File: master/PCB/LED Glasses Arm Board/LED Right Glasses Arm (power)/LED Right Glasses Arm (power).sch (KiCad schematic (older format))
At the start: 24 parts, among them J1 Conn_01x02_Male, J2 Conn_01x01_Male, J3 Conn_01x01_Male, Q1 TP0610T, SW1 SW_SPST, U1 TPS63060

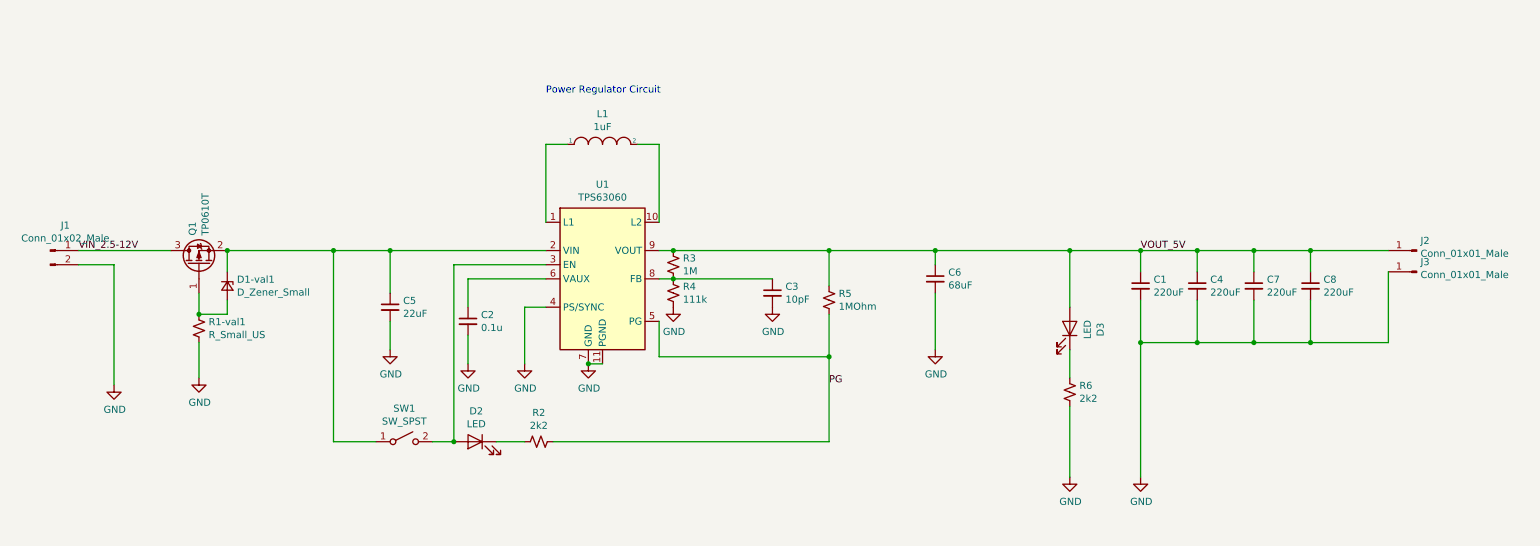
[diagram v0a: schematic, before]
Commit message: Updated with all components with links
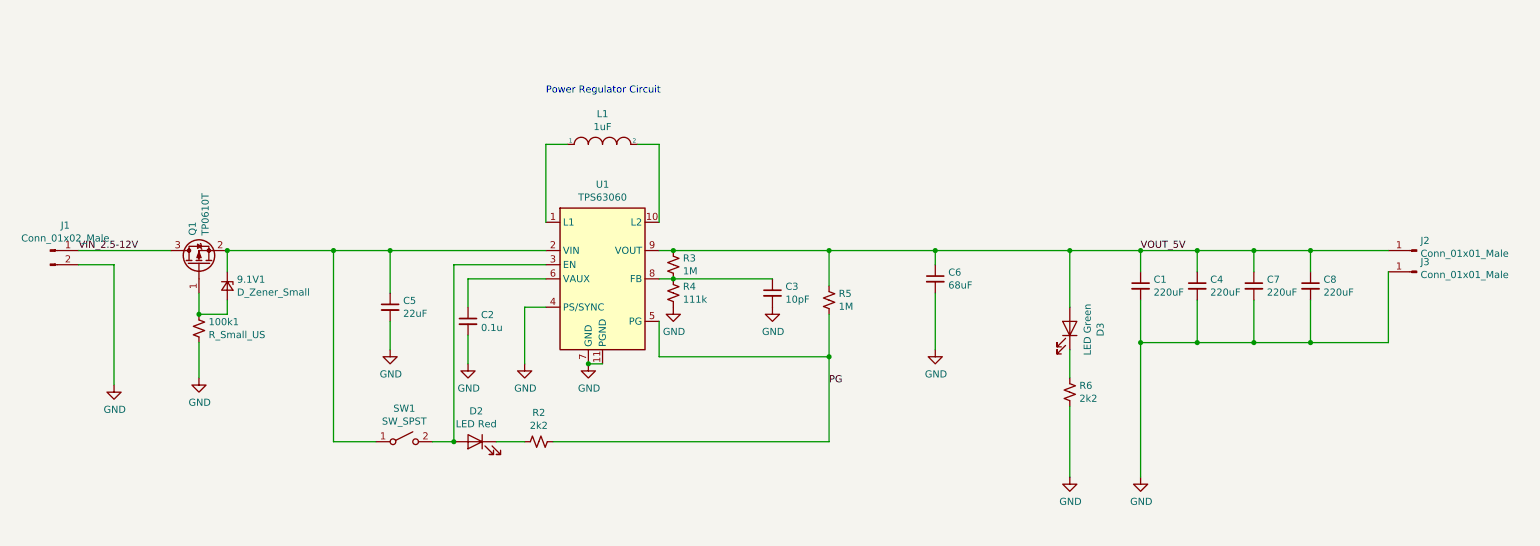
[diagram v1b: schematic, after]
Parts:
- 100k1: renamed from R1-val1; Digikey Link (none) -> https://www.digikey.com.au/product-detail/en/susumu/RR0816P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
- 9.1V1: renamed from D1-val1; Digikey link (none) -> https://www.digikey.com.au/product-detail/en/comchip-techno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
- D2: value LED -> LED Red; Digikey Link (none) -> https://www.digikey.com.au/product-detail/en/lite-on-inc/LT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
- D3: value LED -> LED Green; Digikey Link (none) -> https://www.digikey.com.au/product-detail/en/lite-on-inc/LT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
- L1: footprint Inductor_SMD:L_Coilcraft_XxL4020 -> sft:SRN4018TA; Digikey (none) -> https://www.digikey.com/en/products/detail/bourns-inc/SRN40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; Link XFL4020-102MEC -> (none); Old product (none) -> XFL4020-102MEC; element14 https://au.element14.com/coilcraft/xfl4020-102mec/inductor-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 -> (none)
- Q1: Link https://au.element14.com/vishay/si2315bds-t1-ge3/p-channel-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 -> (none)
- R2, R6: Digikey Link (none) -> https://www.digikey.com.au/product-detail/en/te-connectivit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
- R4: footprint Resistor_SMD:R_0603_1608Metric -> Resistor_SMD:R_0805_2012Metric; Digikey Link (none) -> https://www.digikey.com.au/product-detail/en/vishay-thin-fi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
- R5: value 1MOhm -> 1M
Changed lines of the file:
@@
 F 0 "L1" H 4750 3515 50  0000 C CNN
 F 1 "1uF" H 4750 3424 50  0000 C CNN
-F 2 "Inductor_SMD:L_Coilcraft_XxL4020" H 4750 3300 50  0001 C CNN
-F 3 "http://www.farnell.com/datasheets/1682010.pdf" H 4750 3300 50  0001 C CNN
-F 4 "XFL4020-102MEC" H 4750 3300 50  0001 C CNN "Link"
-F 5 "https://au.element14.com/coilcraft/xfl4020-102mec/inductor-1uh-11a-20-pwr-64mhz/dp/2289214?st=xfl4020-102mec" H 4750 3300 50  0001 C CNN "element14"
+F 2 "sft:SRN4018TA" H 4750 3300 50  0001 C CNN
+F 3 "https://www.bourns.com/docs/Product-Datasheets/SRN4018TA.pdf" H 4750 3300 50  0001 C CNN
+F 4 "XFL4020-102MEC" H 4750 3300 50  0001 C CNN "Old product"
+F 5 "https://www.digikey.com/en/products/detail/bourns-inc/SRN4018TA-1R0M/6565079" H 4750 3300 50  0001 C CNN "Digikey"
 	1    4750 3300
 	1    0    0    -1
@@
 F 1 "1M" H 5318 4105 50  0000 L CNN
 F 2 "Resistor_SMD:R_0603_1608Metric" H 5250 4150 50  0001 C CNN
-F 3 "~" H 5250 4150 50  0001 C CNN
+F 3 "https://www.yageo.com/upload/media/product/productsearch/datasheet/rchip/PYu-RT_1-to-0.01_RoHS_L_12.pdf" H 5250 4150 50  0001 C CNN
 F 4 "https://www.digikey.com.au/product-detail/en/yageo/RT0603BRD071ML/YAG4498CT-ND/6616654" H 5250 4150 50  0001 C CNN "Digikey Link"
 	1    5250 4150
@@
 F 0 "R4" H 5318 4396 50  0000 L CNN
 F 1 "111k" H 5318 4305 50  0000 L CNN
-F 2 "Resistor_SMD:R_0603_1608Metric" H 5250 4350 50  0001 C CNN
-F 3 "~" H 5250 4350 50  0001 C CNN
+F 2 "Resistor_SMD:R_0805_2012Metric" H 5250 4350 50  0001 C CNN
+F 3 "https://www.vishay.com/docs/60026/ptn.pdf" H 5250 4350 50  0001 C CNN
+F 4 "https://www.digikey.com.au/product-detail/en/vishay-thin-film/PTN0805E1113BST1/764-1475-6-ND/7103531" H 5250 4350 50  0001 C CNN "Digikey Link"
 	1    5250 4350
 	1    0    0    -1
@@
 P 6350 4400
 F 0 "R5" H 6418 4446 50  0000 L CNN
-F 1 "1MOhm" H 6418 4355 50  0000 L CNN
+F 1 "1M" H 6418 4355 50  0000 L CNN
 F 2 "Resistor_SMD:R_0603_1608Metric" H 6350 4400 50  0001 C CNN
-F 3 "~" H 6350 4400 50  0001 C CNN
+F 3 "https://www.yageo.com/upload/media/product/productsearch/datasheet/rchip/PYu-RT_1-to-0.01_RoHS_L_12.pdf" H 6350 4400 50  0001 C CNN
 F 4 "https://www.digikey.com.au/product-detail/en/yageo/RT0603BRD071ML/YAG4498CT-ND/6616654" H 6350 4400 50  0001 C CNN "Digikey Link"
 	1    6350 4400
@@
 P 8050 4600
 F 0 "D3" H 8042 4816 50  0000 C CNN
-F 1 "LED" H 8042 4725 50  0000 C CNN
+F 1 "LED Green" H 8042 4725 50  0000 C CNN
 F 2 "LED_SMD:LED_0603_1608Metric" H 8050 4600 50  0001 C CNN
-F 3 "~" H 8050 4600 50  0001 C CNN
+F 3 "https://optoelectronics.liteon.com/upload/download/DS22-2000-226/LTST-S270KGKT.pdf" H 8050 4600 50  0001 C CNN
+F 4 "https://www.digikey.com.au/product-detail/en/lite-on-inc/LTST-S270KGKT/160-1478-1-ND/386892" H 8050 4600 50  0001 C CNN "Digikey Link"
 	1    8050 4600
 	0    1    -1   0
@@
 F 1 "2k2" H 8118 5005 50  0000 L CNN
 F 2 "Resistor_SMD:R_0603_1608Metric" H 8050 5050 50  0001 C CNN
-F 3 "~" H 8050 5050 50  0001 C CNN
+F 3 "https://www.te.com/commerce/DocumentDelivery/DDEController?Action=srchrtrv&DocNm=1773204-3&DocType=DS&DocLang=English" H 8050 5050 50  0001 C CNN
+F 4 "https://www.digikey.com.au/product-detail/en/te-connectivity-passive-product/CRGCQ0603J2K2/A130093CT-ND/8577925" H 8050 5050 50  0001 C CNN "Digikey Link"
 	1    8050 5050
 	1    0    0    -1
@@
 P 3850 5400
 F 0 "D2" H 3842 5616 50  0000 C CNN
-F 1 "LED" H 3842 5525 50  0000 C CNN
+F 1 "LED Red" H 3842 5525 50  0000 C CNN
 F 2 "LED_SMD:LED_0603_1608Metric" H 3850 5400 50  0001 C CNN
-F 3 "~" H 3850 5400 50  0001 C CNN
+F 3 "https://optoelectronics.liteon.com/upload/download/DS22-2000-210/LTST-S270KRKT.pdf" H 3850 5400 50  0001 C CNN
+F 4 "https://www.digikey.com.au/product-detail/en/lite-on-inc/LTST-S270KRKT/160-1479-1-ND/386894" H 3850 5400 50  0001 C CNN "Digikey Link"
 	1    3850 5400
 	-1   0    0    -1
@@
 F 1 "2k2" V 4414 5400 50  0000 C CNN
 F 2 "Resistor_SMD:R_0603_1608Metric" H 4300 5400 50  0001 C CNN
-F 3 "~" H 4300 5400 50  0001 C CNN
+F 3 "https://www.te.com/commerce/DocumentDelivery/DDEController?Action=srchrtrv&DocNm=1773204-3&DocType=DS&DocLang=English" H 4300 5400 50  0001 C CNN
+F 4 "https://www.digikey.com.au/product-detail/en/te-connectivity-passive-product/CRGCQ0603J2K2/A130093CT-ND/8577925" V 4300 5400 50  0001 C CNN "Digikey Link"
 	1    4300 5400
 	0    -1   -1   0
@@
 	4400 5400 6350 5400
 $Comp
-L Device:D_Zener_Small D1-val1
+L Device:D_Zener_Small 9.1V1
 U 1 1 5F7F1725
 P 2100 4300
-F 0 "D1-val1" V 2054 4368 50  0000 L CNN
+F 0 "9.1V1" V 2054 4368 50  0000 L CNN
 F 1 "D_Zener_Small" V 2145 4368 50  0000 L CNN
 F 2 "Diode_SMD:D_0603_1608Metric" V 2100 4300 50  0001 C CNN
-F 3 "~" V 2100 4300 50  0001 C CNN
+F 3 "https://media.digikey.com/pdf/Data%20Sheets/Comchip%20PDFs/CZRU52C2-CZRU52C39_DS.pdf" V 2100 4300 50  0001 C CNN
+F 4 "https://www.digikey.com.au/product-detail/en/comchip-technology/CZRU52C9V1/641-1035-1-ND/1121157" V 2100 4300 50  0001 C CNN "Digikey link"
 	1    2100 4300
 	0    1    1    0
 $EndComp
 $Comp
-L Device:R_Small_US R1-val1
+L Device:R_Small_US 100k1
 U 1 1 5F7F24DD
 P 1900 4600
-F 0 "R1-val1" H 1968 4646 50  0000 L CNN
+F 0 "100k1" H 1968 4646 50  0000 L CNN
 F 1 "R_Small_US" H 1968 4555 50  0000 L CNN
 F 2 "Resistor_SMD:R_0603_1608Metric" H 1900 4600 50  0001 C CNN
-F 3 "~" H 1900 4600 50  0001 C CNN
+F 3 "https://www.susumu.co.jp/common/pdf/n_catalog_partition05_en.pdf" H 1900 4600 50  0001 C CNN
+F 4 "https://www.digikey.com.au/product-detail/en/susumu/RR0816P-104-D/RR08P100KDCT-ND/432772" H 1900 4600 50  0001 C CNN "Digikey Link"
 	1    1900 4600
 	1    0    0    -1
@@
 F 1 "TP0610T" H 2106 4105 50  0000 L CNN
 F 2 "Package_TO_SOT_SMD:SOT-23" H 2100 4075 50  0001 L CIN
-F 3 "http://www.farnell.com/datasheets/2046951.pdf" H 1900 4150 50  0001 L CNN
-F 4 "https://au.element14.com/vishay/si2315bds-t1-ge3/p-channel-mosfet/dp/1867177?st=p%20channel%20mosfet" H 1900 4150 50  0001 C CNN "Link"
-F 5 "https://www.digikey.com.au/product-detail/en/vishay-siliconix/SI2315BDS-T1-GE3/SI2315BDS-T1-GE3CT-ND/6595280" H 1900 4150 50  0001 C CNN "Digikey Link"
+F 3 "https://www.vishay.com/docs/72014/72014.pdf" H 1900 4150 50  0001 L CNN
+F 4 "https://www.digikey.com.au/product-detail/en/vishay-siliconix/SI2315BDS-T1-GE3/SI2315BDS-T1-GE3CT-ND/6595280" H 1900 4150 50  0001 C CNN "Digikey Link"
 	1    1900 4150
 	0    -1   -1   0

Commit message: Added digikey link for regulator
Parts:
- U1: Digikey Link (none) -> https://www.digikey.com.au/product-detail/en/texas-instrume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
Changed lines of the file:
@@
 F 2 "Package_SON:Texas_S-PWSON-N10" H 4750 3600 50  0001 C CNN
 F 3 "http://www.ti.com/lit/ds/symlink/tps63060.pdf" H 4750 4250 50  0001 C CNN
+F 4 "https://www.digikey.com.au/product-detail/en/texas-instruments/TPS63060DSCR/296-30204-1-ND/2834996" H 4750 4250 50  0001 C CNN "Digikey Link"
 	1    4750 4250
 	1    0    0    -1

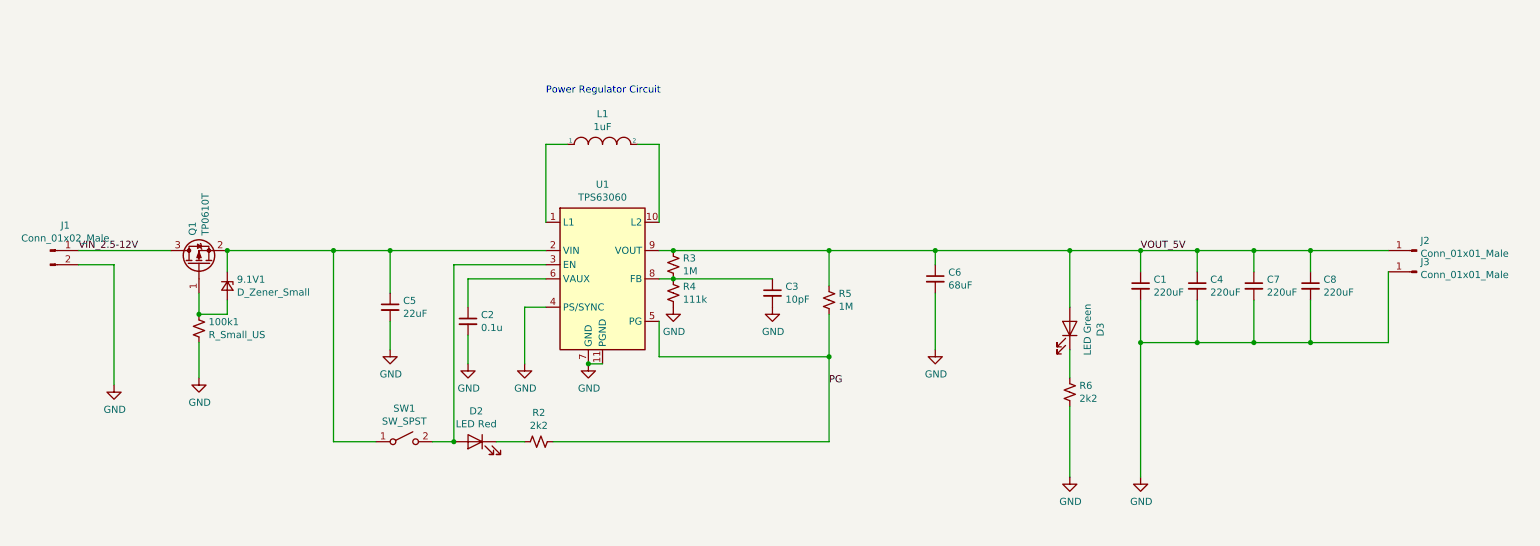
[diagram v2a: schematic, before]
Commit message: added labels, new zener diode, began layout
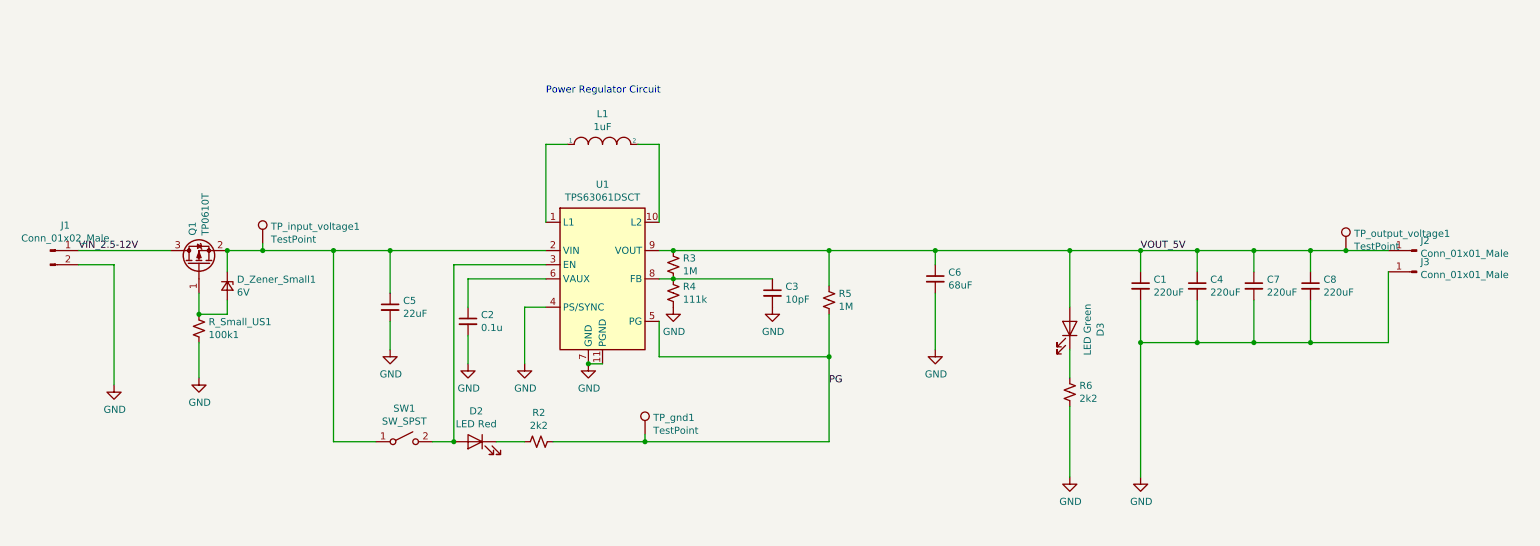
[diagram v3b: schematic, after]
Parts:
- added TP_gnd1, TP_input_voltage1, TP_output_voltage1: TestPoint, Connector_PinHeader_1.00mm:PinHeader_1x01_P1.00mm_Vertical_SMD_CUSTOM, symbol Connector:TestPoint
- D_Zener_Small1: renamed from 9.1V1; value D_Zener_Small -> 6V; footprint Diode_SMD:D_0603_1608Metric -> Diode_SMD:D_SOD-123; Digikey link https://www.digikey.com.au/product-detail/en/comchip-techno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 -> https://www.digikey.com.au/product-detail/en/vishay-general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
- R_Small_US1: renamed from 100k1; value R_Small_US -> 100k1
- U1: value TPS63060 -> TPS63061DSCT; Digikey Link https://www.digikey.com.au/product-detail/en/texas-instruments/TPS63060DSCR/296-30204-1-ND/2834996 -> https://www.digikey.com.au/product-detail/en/texas-instruments/TPS63061DSCT/296-30179-1-ND/2812734
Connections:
- net PG: now also TP_gnd1.1
- net VOUT_5V: now also TP_output_voltage1.1
- net at C5.1, D_Zener_Small1.1 (K), Q1.2 (S)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: now also TP_input_voltage1.1
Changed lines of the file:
@@
 P 4750 4250
 F 0 "U1" H 4750 4917 50  0000 C CNN
-F 1 "TPS63060" H 4750 4826 50  0000 C CNN
+F 1 "TPS63061DSCT" H 4750 4826 50  0000 C CNN
 F 2 "Package_SON:Texas_S-PWSON-N10" H 4750 3600 50  0001 C CNN
-F 3 "http://www.ti.com/lit/ds/symlink/tps63060.pdf" H 4750 4250 50  0001 C CNN
-F 4 "https://www.digikey.com.au/product-detail/en/texas-instruments/TPS63060DSCR/296-30204-1-ND/2834996" H 4750 4250 50  0001 C CNN "Digikey Link"
+F 3 "https://www.ti.com/lit/ds/symlink/tps63061.pdf?HQS=dis-dk-null-digikeymode-dsf-pf-null-wwe&ts=1618215570038&ref_url=https%253A%252F%252Fwww.digikey.com.au%252F" H 4750 4250 50  0001 C CNN
+F 4 "https://www.digikey.com.au/product-detail/en/texas-instruments/TPS63061DSCT/296-30179-1-ND/2812734" H 4750 4250 50  0001 C CNN "Digikey Link"
 	1    4750 4250
 	1    0    0    -1
@@
 	6350 4800 6350 5400
 Wire Wire Line
-	4400 5400 6350 5400
-$Comp
-L Device:D_Zener_Small 9.1V1
+	4400 5400 5050 5400
+$Comp
+L Device:D_Zener_Small D_Zener_Small1
 U 1 1 5F7F1725
 P 2100 4300
-F 0 "9.1V1" V 2054 4368 50  0000 L CNN
-F 1 "D_Zener_Small" V 2145 4368 50  0000 L CNN
-F 2 "Diode_SMD:D_0603_1608Metric" V 2100 4300 50  0001 C CNN
-F 3 "https://media.digikey.com/pdf/Data%20Sheets/Comchip%20PDFs/CZRU52C2-CZRU52C39_DS.pdf" V 2100 4300 50  0001 C CNN
-F 4 "https://www.digikey.com.au/product-detail/en/comchip-technology/CZRU52C9V1/641-1035-1-ND/1121157" V 2100 4300 50  0001 C CNN "Digikey link"
+F 0 "D_Zener_Small1" V 2054 4368 50  0000 L CNN
+F 1 "6V" V 2145 4368 50  0000 L CNN
+F 2 "Diode_SMD:D_SOD-123" V 2100 4300 50  0001 C CNN
+F 3 "https://www.vishay.com/docs/85774/mmsz5225.pdf" V 2100 4300 50  0001 C CNN
+F 4 "https://www.digikey.com.au/product-detail/en/vishay-general-semiconductor-diodes-division/MMSZ5233B-E3-08/112-MMSZ5233B-E3-08CT-ND/8565146" V 2100 4300 50  0001 C CNN "Digikey link"
 	1    2100 4300
 	0    1    1    0
 $EndComp
 $Comp
-L Device:R_Small_US 100k1
+L Device:R_Small_US R_Small_US1
 U 1 1 5F7F24DD
 P 1900 4600
-F 0 "100k1" H 1968 4646 50  0000 L CNN
-F 1 "R_Small_US" H 1968 4555 50  0000 L CNN
+F 0 "R_Small_US1" H 1968 4646 50  0000 L CNN
+F 1 "100k1" H 1968 4555 50  0000 L CNN
 F 2 "Resistor_SMD:R_0603_1608Metric" H 1900 4600 50  0001 C CNN
 F 3 "https://www.susumu.co.jp/common/pdf/n_catalog_partition05_en.pdf" H 1900 4600 50  0001 C CNN
@@
 Wire Wire Line
 	1900 4500 2100 4500
-Wire Wire Line
-	2100 4500 2100 4400
 $Comp
 L Transistor_FET:TP0610T Q1
@@
 $EndComp
 Wire Wire Line
-	2100 4050 2850 4050
-Wire Wire Line
-	2100 4200 2100 4050
-Connection ~ 2100 4050
+	2100 4050 2350 4050
 Wire Wire Line
 	1900 4350 1900 4500
@@
 	1    0    0    -1
 $EndComp
-Connection ~ 3250 4050
 Wire Wire Line
 	3250 4050 4350 4050
@@
 Connection ~ 9750 4050
 Wire Wire Line
-	9750 4050 10300 4050
+	9750 4050 10000 4050
+Connection ~ 3250 4050
+$Comp
+L Connector:TestPoint TP_output_voltage1
+U 1 1 60740989
+P 10000 4050
+F 0 "TP_output_voltage1" H 10058 4170 50  0000 L CNN
+F 1 "TestPoint" H 10058 4079 50  0000 L CNN
+F 2 "Connector_PinHeader_1.00mm:PinHeader_1x01_P1.00mm_Vertical_SMD_CUSTOM" H 10200 4050 50  0001 C CNN
+F 3 "~" H 10200 4050 50  0001 C CNN
+	1    10000 4050
+	1    0    0    -1
+$EndComp
+Connection ~ 10000 4050
+Wire Wire Line
+	10000 4050 10300 4050
+$Comp
+L Connector:TestPoint TP_input_voltage1
+U 1 1 60741617
+P 2350 4000
+F 0 "TP_input_voltage1" H 2408 4120 50  0000 L CNN
+F 1 "TestPoint" H 2408 4029 50  0000 L CNN
+F 2 "Connector_PinHeader_1.00mm:PinHeader_1x01_P1.00mm_Vertical_SMD_CUSTOM" H 2550 4000 50  0001 C CNN
+F 3 "~" H 2550 4000 50  0001 C CNN
+	1    2350 4000
+	1    0    0    -1
+$EndComp
+$Comp
+L Connector:TestPoint TP_gnd1
+U 1 1 60742752
+P 5050 5350
+F 0 "TP_gnd1" H 5108 5470 50  0000 L CNN
+F 1 "TestPoint" H 5108 5379 50  0000 L CNN
+F 2 "Connector_PinHeader_1.00mm:PinHeader_1x01_P1.00mm_Vertical_SMD_CUSTOM" H 5250 5350 50  0001 C CNN
+F 3 "~" H 5250 5350 50  0001 C CNN
+	1    5050 5350
+	1    0    0    -1
+$EndComp
+Wire Wire Line
+	2100 4500 2100 4400
+Connection ~ 2100 4050
+Wire Wire Line
+	2100 4200 2100 4050
+Wire Wire Line
+	2350 4000 2350 4050
+Connection ~ 2350 4050
+Wire Wire Line
+	2350 4050 2850 4050
+Wire Wire Line
+	5050 5350 5050 5400
+Connection ~ 5050 5400
+Wire Wire Line
+	5050 5400 6350 5400
 $EndSCHEMATC

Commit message: updated board
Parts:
- removed R5: 1M, Resistor_SMD:R_0603_1608Metric, symbol Device:R_Small_US
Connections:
- net GND: now also R2.2, TP_gnd1.1
- removed net PG: R2.2, TP_gnd1.1, U1.5 (PG)
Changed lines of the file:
@@
 	5150 3300 5150 3850
-Wire Wire Line
-	5150 4800 6350 4800
 Wire Wire Line
 	5150 4050 5250 4050
@@
 Connection ~ 5250 4050
 Wire Wire Line
-	5250 4050 6350 4050
-Wire Wire Line
 	5150 4250 5250 4250
 $Comp
@@
 	1    0    0    -1
 $EndComp
-Wire Wire Line
-	5150 4550 5150 4800
 $Comp
 L power:GND #PWR0106
@@
 $EndComp
 $Comp
-L Device:R_Small_US R5
-U 1 1 5F4BBDC6
-P 6350 4400
-F 0 "R5" H 6418 4446 50  0000 L CNN
-F 1 "1M" H 6418 4355 50  0000 L CNN
-F 2 "Resistor_SMD:R_0603_1608Metric" H 6350 4400 50  0001 C CNN
-F 3 "https://www.yageo.com/upload/media/product/productsearch/datasheet/rchip/PYu-RT_1-to-0.01_RoHS_L_12.pdf" H 6350 4400 50  0001 C CNN
-F 4 "https://www.digikey.com.au/product-detail/en/yageo/RT0603BRD071ML/YAG4498CT-ND/6616654" H 6350 4400 50  0001 C CNN "Digikey Link"
-	1    6350 4400
-	1    0    0    -1
-$EndComp
-Wire Wire Line
-	6350 4050 6350 4300
-Wire Wire Line
-	6350 4500 6350 4800
-Connection ~ 6350 4050
-$Comp
 L power:GND #PWR0108
 U 1 1 5F4BEA89
@@
 Text Label 8550 4050 0    50   ~ 0
 VOUT_5V
-Connection ~ 6350 4800
-Text Label 6350 5000 0    50   ~ 0
-PG
 Wire Wire Line
 	4350 4150 3700 4150
@@
 Connection ~ 3700 5400
 Wire Wire Line
-	6350 4800 6350 5400
-Wire Wire Line
 	4400 5400 5050 5400
 $Comp
@@
 $EndComp
 Wire Wire Line
-	6350 4050 7100 4050
-Wire Wire Line
 	7100 4050 7100 4150
 Connection ~ 7100 4050
@@
 Wire Wire Line
 	2350 4050 2850 4050
+$Comp
+L power:GND #PWR0112
+U 1 1 6075711B
+P 5050 5750
+F 0 "#PWR0112" H 5050 5500 50  0001 C CNN
+F 1 "GND" H 5055 5577 50  0000 C CNN
+F 2 "" H 5050 5750 50  0001 C CNN
+F 3 "" H 5050 5750 50  0001 C CNN
+	1    5050 5750
+	1    0    0    -1
+$EndComp
 Wire Wire Line
 	5050 5350 5050 5400
 Connection ~ 5050 5400
 Wire Wire Line
-	5050 5400 6350 5400
+	5050 5400 5050 5750
+Wire Wire Line
+	5250 4050 7100 4050
 $EndSCHEMATC
